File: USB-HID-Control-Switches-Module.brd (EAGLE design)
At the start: 58 x 22.5 mm, 3 parts, among them M1 PRO_MICRO_SMD

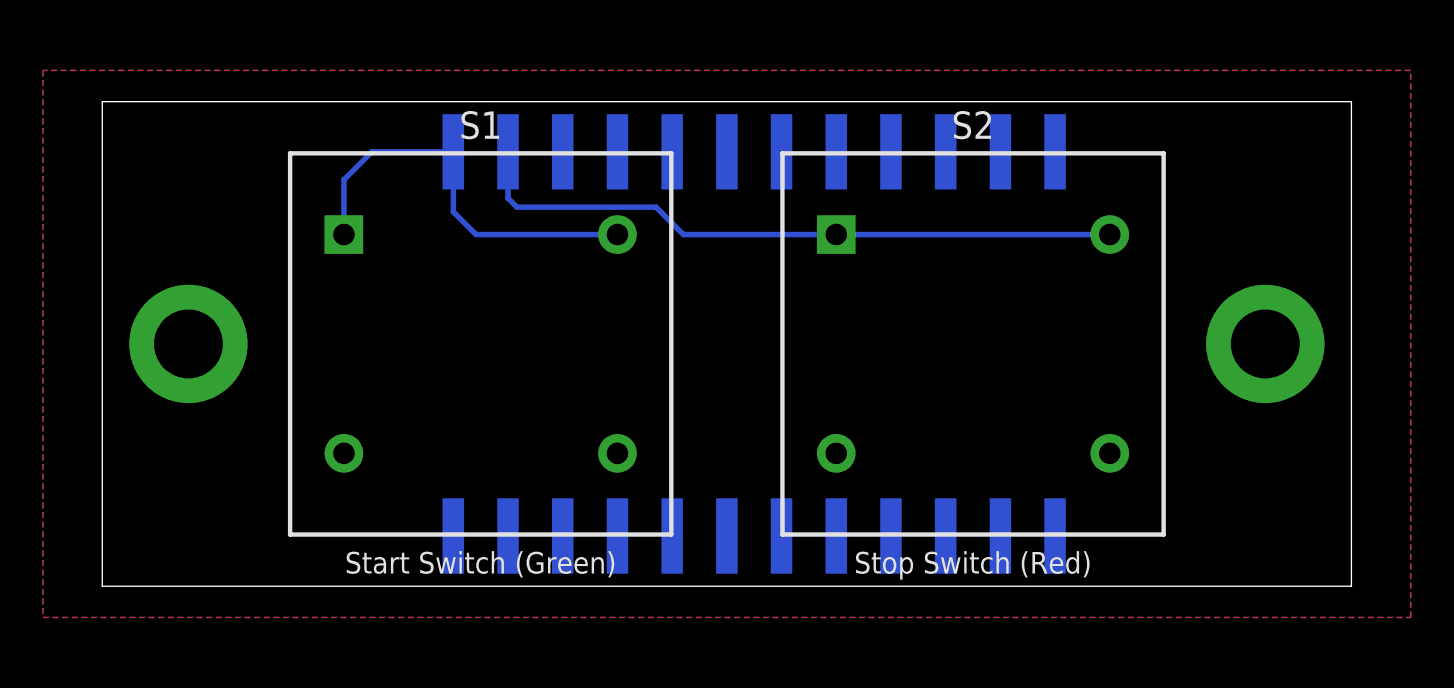
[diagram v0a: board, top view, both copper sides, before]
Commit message: Change the mounting orientation of the microcontroller board
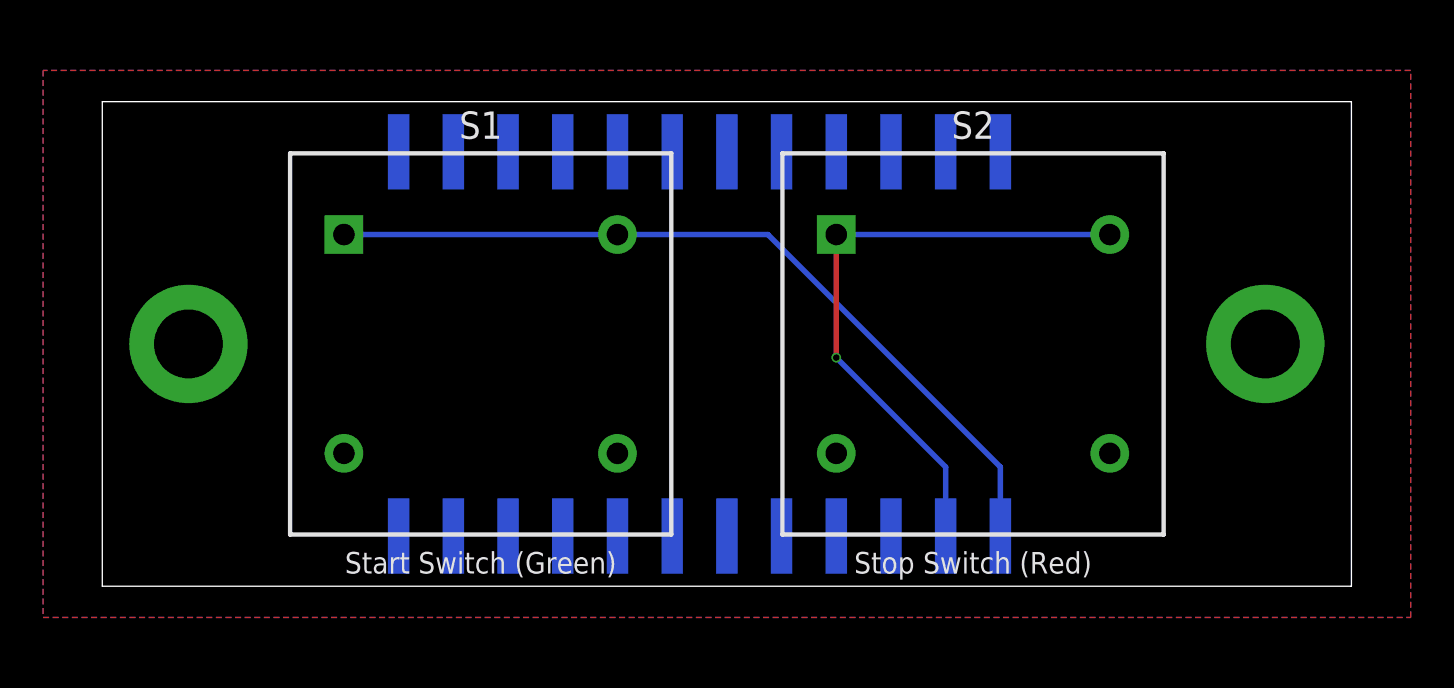
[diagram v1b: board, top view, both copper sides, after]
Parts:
- moved M1 2.54 mm to (-1.27, 0.00), turned to 90 degrees
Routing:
- net START_BUTTON: track 19.0 -> 38.2 mm
- net STOP_BUTTON: track 30.8 -> 28.8 mm, vias 0 -> 1
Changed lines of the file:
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@@
 <setting verticaltext="up"/>
 </settings>
-<grid distance="50" unitdist="mil" unit="mm" style="lines" multiple="1" display="yes" altdistance="1.27" altunitdist="mm" altunit="mm"/>
+<grid distance="25" unitdist="mil" unit="mil" style="lines" multiple="1" display="yes" altdistance="1.27" altunitdist="mm" altunit="mm"/>
 <layers>
 <layer number="1" name="Top" color="4" fill="1" visible="yes" active="yes"/>
@@
 <dimension x1="25" y1="0" x2="-25" y2="0" x3="0" y3="15" textsize="1.778" layer="48"/>
 <dimension x1="-25" y1="11.25" x2="-25" y2="0" x3="-35.8776875" y3="5.625" textsize="1.778" layer="48"/>
-<wire x1="-13.335" y1="8.89" x2="-16.51" y2="8.89" width="0.1524" layer="22"/>
-<wire x1="-16.51" y1="8.89" x2="-16.51" y2="3.9" width="0.1524" layer="22"/>
-<wire x1="-16.51" y1="3.9" x2="-16.51" y2="-3.9" width="0.1524" layer="22"/>
-<wire x1="-16.51" y1="-3.9" x2="-16.51" y2="-8.89" width="0.1524" layer="22"/>
-<wire x1="-16.51" y1="-8.89" x2="-13.335" y2="-8.89" width="0.1524" layer="22"/>
-<wire x1="15.875" y1="8.89" x2="16.51" y2="8.89" width="0.1524" layer="22"/>
-<wire x1="16.51" y1="8.89" x2="16.51" y2="-8.89" width="0.1524" layer="22"/>
-<wire x1="16.51" y1="-8.89" x2="15.875" y2="-8.89" width="0.1524" layer="22"/>
+<wire x1="16.51" y1="8.89" x2="16.51" y2="3.9" width="0.1524" layer="22"/>
+<wire x1="16.51" y1="3.9" x2="16.51" y2="-3.9" width="0.1524" layer="22"/>
+<wire x1="16.51" y1="-3.9" x2="16.51" y2="-8.89" width="0.1524" layer="22"/>
 <rectangle x1="-28.575" y1="-10.795" x2="-17.145" y2="-6.985" layer="22"/>
 <text x="-22.86" y="-6.35" size="0.8" layer="22" rot="MR0" align="center">Serial No.</text>
 <rectangle x1="17.145" y1="-10.795" x2="28.575" y2="-6.985" layer="22"/>
 <text x="22.86" y="-6.35" size="0.8" layer="22" rot="MR0" align="center">Production Date</text>
-<wire x1="-16.51" y1="3.9" x2="-17.39" y2="3.9" width="0.1524" layer="22"/>
-<wire x1="-17.39" y1="3.9" x2="-17.39" y2="-3.9" width="0.1524" layer="22"/>
-<wire x1="-17.39" y1="-3.9" x2="-16.51" y2="-3.9" width="0.1524" layer="22"/>
+<wire x1="16.51" y1="3.9" x2="17.39" y2="3.9" width="0.1524" layer="22"/>
+<wire x1="17.39" y1="3.9" x2="17.39" y2="-3.9" width="0.1524" layer="22"/>
+<wire x1="17.39" y1="-3.9" x2="16.51" y2="-3.9" width="0.1524" layer="22"/>
+<wire x1="-16.51" y1="8.89" x2="-16.51" y2="-8.89" width="0.1524" layer="22"/>
+<wire x1="13.97" y1="-8.89" x2="16.51" y2="-8.89" width="0.1524" layer="22"/>
+<wire x1="13.335" y1="8.89" x2="16.51" y2="8.89" width="0.1524" layer="22"/>
+<wire x1="-15.875" y1="8.89" x2="-16.51" y2="8.89" width="0.1524" layer="22"/>
+<wire x1="-16.51" y1="-8.89" x2="-15.875" y2="-8.89" width="0.1524" layer="22"/>
 </plain>
 <attributes>
@@
 <attribute name="NAME" x="-11.43" y="10.16" size="1.27" layer="25" ratio="10" rot="R180" align="center"/>
 </element>
-<element name="M1" library="Arduino" package="PRO_MICRO_SMD" value="PRO_MICRO_SMD" x="1.27" y="0" smashed="yes" rot="MR270">
-<attribute name="NAME" x="-18.415" y="0" size="1" layer="26" ratio="10" rot="MR270" align="center"/>
+<element name="M1" library="Arduino" package="PRO_MICRO_SMD" value="PRO_MICRO_SMD" x="-1.27" y="0" smashed="yes" rot="MR90">
+<attribute name="NAME" x="18.415" y="0" size="1" layer="26" ratio="10" rot="MR90" align="center"/>
 </element>
 </elements>
@@
 <contactref element="S1" pad="1"/>
 <contactref element="M1" pad="1"/>
-<wire x1="-16.48" y1="8.92" x2="-17.78" y2="7.62" width="0.254" layer="16"/>
-<wire x1="-17.78" y1="5.08" x2="-17.78" y2="7.62" width="0.254" layer="16"/>
-<wire x1="-16.48" y1="8.92" x2="-12.7" y2="8.92" width="0.254" layer="16"/>
-<wire x1="-11.6488125" y1="5.08" x2="-12.7" y2="6.1311875" width="0.254" layer="16"/>
-<wire x1="-12.7" y1="8.92" x2="-12.7" y2="6.1311875" width="0.254" layer="16"/>
-<wire x1="-11.6488125" y1="5.08" x2="-5.08" y2="5.08" width="0.254" layer="16"/>
+<wire x1="-17.78" y1="5.08" x2="-5.08" y2="5.08" width="0.254" layer="16"/>
+<wire x1="-5.08" y1="5.08" x2="1.905" y2="5.08" width="0.254" layer="16"/>
+<wire x1="1.905" y1="5.08" x2="12.7" y2="-5.715" width="0.254" layer="16"/>
+<wire x1="12.7" y1="-5.715" x2="12.7" y2="-8.92" width="0.254" layer="16"/>
 </signal>
 <signal name="STOP_BUTTON">
@@
 <contactref element="S2" pad="1"/>
 <contactref element="M1" pad="2"/>
-<wire x1="-9.7438125" y1="6.35" x2="-10.16" y2="6.7661875" width="0.254" layer="16"/>
-<wire x1="-10.16" y1="8.92" x2="-10.16" y2="6.7661875" width="0.254" layer="16"/>
-<wire x1="-2.01394375" y1="5.08" x2="5.08" y2="5.08" width="0.254" layer="16"/>
-<wire x1="-3.28394375" y1="6.35" x2="-2.01394375" y2="5.08" width="0.254" layer="16"/>
-<wire x1="-9.7438125" y1="6.35" x2="-3.28394375" y2="6.35" width="0.254" layer="16"/>
-<wire x1="5.08" y1="5.08" x2="17.78" y2="5.08" width="0.254" layer="16"/>
+<wire x1="10.16" y1="-8.92" x2="10.16" y2="-5.715" width="0.254" layer="16"/>
+<wire x1="10.16" y1="-5.715" x2="5.08" y2="-0.635" width="0.254" layer="16"/>
+<wire x1="17.78" y1="5.08" x2="5.08" y2="5.08" width="0.254" layer="16"/>
+<wire x1="5.08" y1="5.08" x2="5.08" y2="-0.635" width="0.254" layer="1"/>
+<via x="5.08" y="-0.635" extent="1-16" drill="0.3"/>
 </signal>
 <signal name="AGND">
@@
 <vertex x="31.75" y="12.7"/>
 </polygon>
-<wire x1="-5.08" y1="-5.08" x2="-5.08" y2="8.92" width="0" layer="19" extent="16-16"/>
 </signal>
 <signal name="SCREW_HOLE1">

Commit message: Additional LED for status check
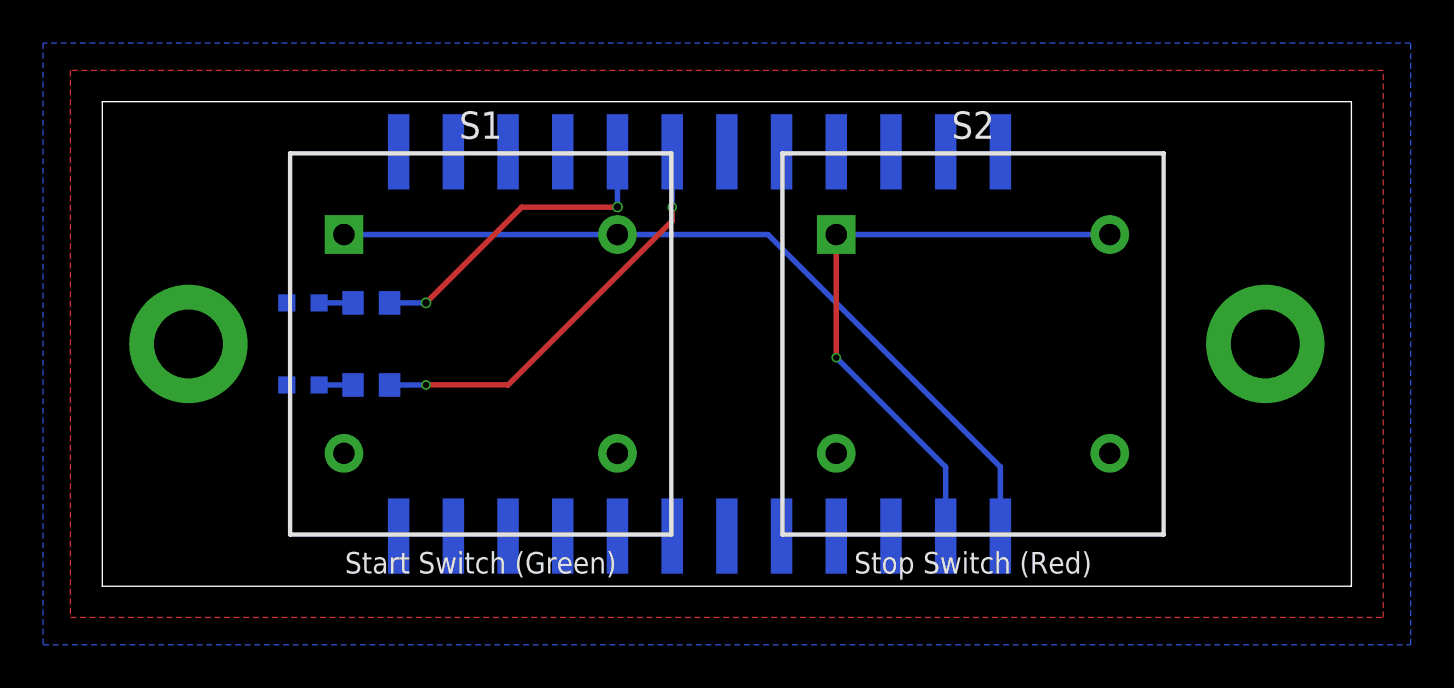
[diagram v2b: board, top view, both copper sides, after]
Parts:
- added LED1: Red, led:SML0603
- added LED2: Green, led:SML0603
- added R1, R2: 2k, rcl:R0603
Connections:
- removed net AGND: M1.23, M1.3, M1.4, S1.3, S1.4, S2.3, S2.4
- new net GND: LED1.C, LED2.C, M1.23, M1.3, M1.4, S1.3, S1.4, S2.3, S2.4
- new net GREEN_LED: M1.18, R2.2
- new net LED1: LED1.A, R1.1
- new net LED2: LED2.A, R2.1
- new net RED_LED: M1.17, R1.2
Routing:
- net GREEN_LED: track 0.00 -> 19.6 mm, vias 0 -> 2
- net RED_LED: track 0.00 -> 15.0 mm, vias 0 -> 2
- net LED2: track 0.00 -> 1.57 mm
- net LED1: track 0.00 -> 1.57 mm
- added copper zone on layer 1, net GND
- added copper zone on layer 16, net GND
- removed copper zone on layer 1, net AGND
- removed copper zone on layer 16, net AGND
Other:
- board text added: "USB-HID Control Switches Module Rev. 1 Designed by Masato Kubotera on May 31, 2023."
- board text removed: "USB-HID Control Switches Module Rev. 1 Designed by Masato Kubotera on May 19, 2023."
